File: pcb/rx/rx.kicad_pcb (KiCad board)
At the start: 2 copper layers, 82.3 x 70.8 mm, 60 parts, among them SW1 SW_SPDT, U1 nice_nano, U2 MPU-6500, U3 QMC5883P, U4 MCP6004, U5 MCP6004, U6 74HC4051

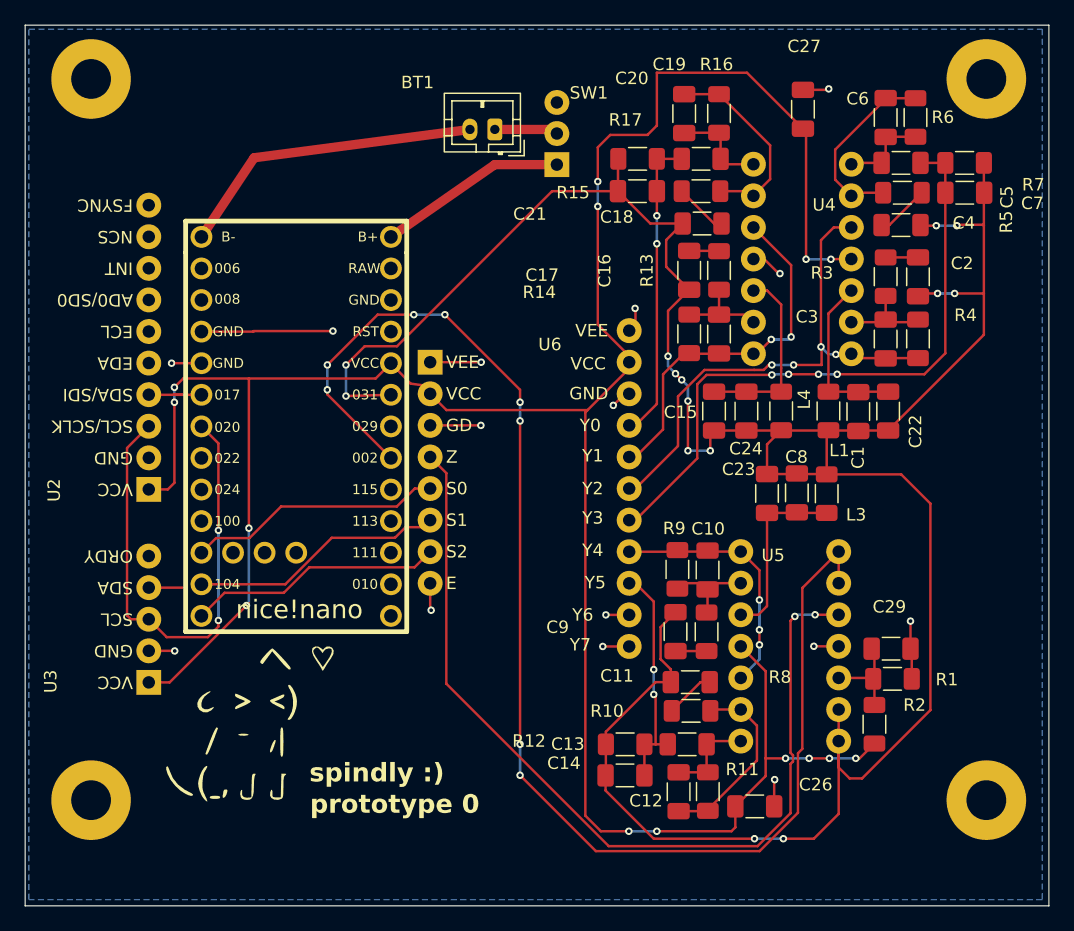
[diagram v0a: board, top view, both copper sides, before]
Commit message: Update Rx board to include anchor
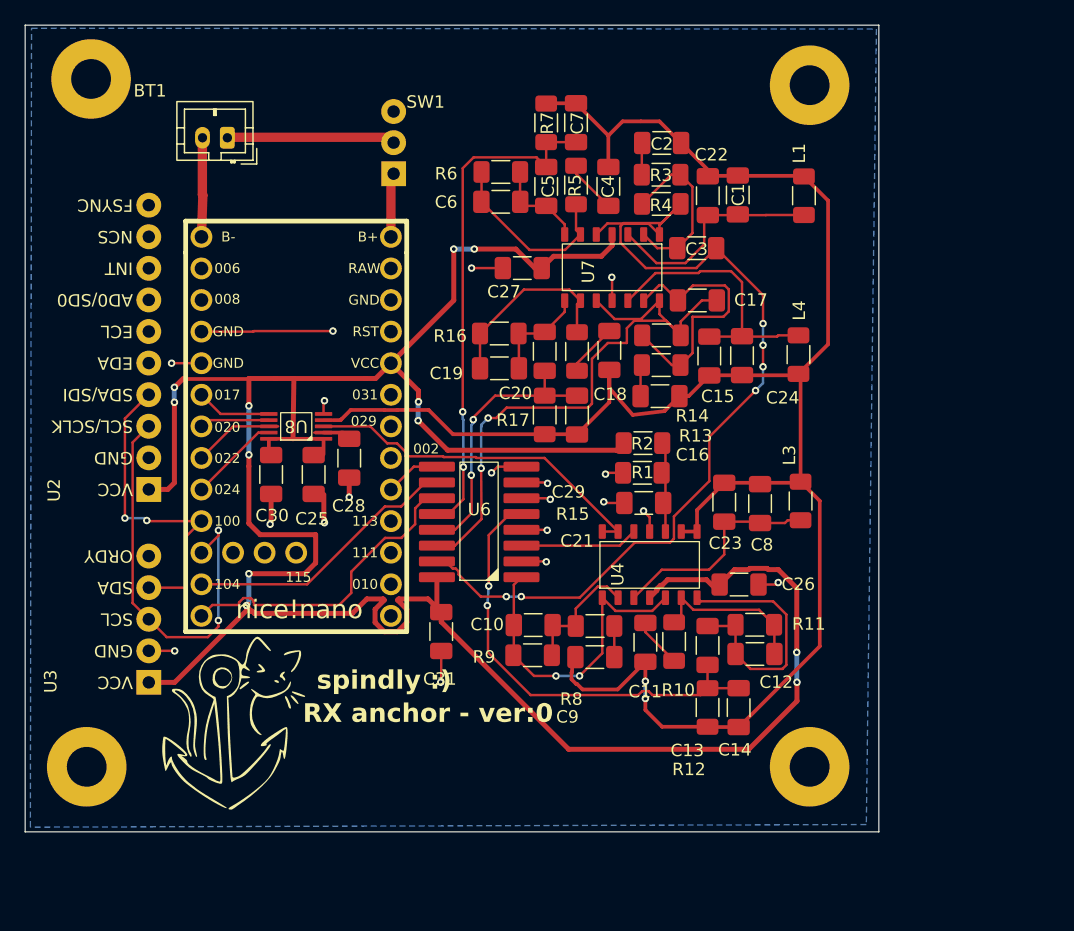
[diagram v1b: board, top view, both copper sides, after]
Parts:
- removed the G*** at (98.3, 83.4)
- removed U5: MCP6004, Library:MCP6004
- added C25: 0.1uF, Capacitor_SMD:C_1206_3216Metric_Pad1.33x1.80mm_HandSolder, F.Cu at (103.9, 63.3)
- added C28: 0.1uF, Capacitor_SMD:C_1206_3216Metric_Pad1.33x1.80mm_HandSolder, F.Cu at (106.8, 62.0)
- added C30: 0.1uF, Capacitor_SMD:C_1206_3216Metric_Pad1.33x1.80mm_HandSolder, F.Cu at (100.5, 63.3)
- added C31: 0.1uF, Capacitor_SMD:C_1206_3216Metric_Pad1.33x1.80mm_HandSolder, F.Cu at (114.2, 75.9)
- added G***: LOGO, Library:cat2_silk, F.Cu at (97.4, 83.3)
- added U7: NCS20034DR2G, Library:NCS20034DR2G, F.Cu at (127.9, 46.7)
- added U8: MCP33131-10-E/MS, Library:MCP33131, F.Cu at (102.5, 59.4)
- U4: value MCP6004 -> NCS20034DR2G; footprint Library:MCP6004 -> Library:NCS20034DR2G
- U6: footprint Library:74HC4051 -> Library:74HC4051-chip
- moved R7 33.8 mm to (122.6, 35.0), turned to 90 degrees
- moved R6 33.6 mm to (119.0, 39.0), turned to 180 degrees
- moved C7 31.8 mm to (125.0, 35.0), turned to -90 degrees
- moved C6 31.7 mm to (119.0, 41.4), turned to 0 degrees
- moved R2 29.3 mm to (130.4, 60.8), turned to 0 degrees
- moved C5 28.6 mm to (122.6, 40.1), turned to -90 degrees
- moved R5 26.3 mm to (125.0, 40.0), turned to 90 degrees
- moved R1 26.1 mm to (130.3, 63.2), turned to 180 degrees
- moved C27 25.9 mm to (120.7, 46.7), turned to 180 degrees
- moved C19 25.3 mm to (118.8, 54.8), turned to 0 degrees
- moved R16 25.0 mm to (118.8, 52.0), turned to 180 degrees
- moved C4 23.7 mm to (127.6, 40.1), turned to -90 degrees
- moved R4 23.3 mm to (131.9, 41.5), turned to 180 degrees
- moved C2 23.3 mm to (131.9, 36.6), turned to 0 degrees
- moved C29 23.1 mm to (130.4, 65.6), turned to 0 degrees
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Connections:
- C1 pad 1: Net-(U4A-+) -> Net-(U7A-+)
- C10 pad 1: Net-(U5A--) -> Net-(U4A--)
- C12 pad 1: Net-(U5B--) -> Net-(U4B--)
- C15 pad 1: Net-(U4D-+) -> Net-(U7D-+)
- C17 pad 1: Net-(U4D--) -> Net-(U7D--)
- C19 pad 1: Net-(U4C--) -> Net-(U7C--)
- C22 pad 1: Net-(U4A-+) -> Net-(U7A-+)
- C23 pad 1: Net-(U5A-+) -> Net-(U4A-+)
- C24 pad 1: Net-(U4D-+) -> Net-(U7D-+)
- C29 pad 2: Net-(U5C-+) -> Net-(U4C-+)
- C3 pad 1: Net-(U4A--) -> Net-(U7A--)
- C6 pad 1: Net-(U4B--) -> Net-(U7B--)
- C8 pad 1: Net-(U5A-+) -> Net-(U4A-+)
- L1 pad 1: Net-(U4A-+) -> Net-(U7A-+)
- L3 pad 1: Net-(U5A-+) -> Net-(U4A-+)
- L4 pad 1: Net-(U4D-+) -> Net-(U7D-+)
- R1 pad 1: Net-(U5C-+) -> Net-(U4C-+)
- R10 pad 1: Net-(U5B--) -> Net-(U4B--)
- R11 pad 2: Net-(U5B--) -> Net-(U4B--)
- R13 pad 1: Net-(U4D--) -> Net-(U7D--)
- R14 pad 2: Net-(U4D--) -> Net-(U7D--)
- R15 pad 1: Net-(U4C--) -> Net-(U7C--)
- R16 pad 2: Net-(U4C--) -> Net-(U7C--)
- R2 pad 2: Net-(U5C-+) -> Net-(U4C-+)
- R3 pad 1: Net-(U4A--) -> Net-(U7A--)
- R4 pad 2: Net-(U4A--) -> Net-(U7A--)
- R5 pad 1: Net-(U4B--) -> Net-(U7B--)
- R6 pad 2: Net-(U4B--) -> Net-(U7B--)
- R8 pad 1: Net-(U5A--) -> Net-(U4A--)
- R9 pad 2: Net-(U5A--) -> Net-(U4A--)
- U1 pad 10: /SELECT_0 -> /SCK
- U1 pad 12: /SELECT_2 -> /SELECT_0
- U1 pad 17: unconnected-(U1-P1.15-Pad17) -> /SELECT_2
- U1 pad 18: /ADC_0 -> unconnected-(U1-AIN0/P0.02-Pad18)
- U1 pad 20: /V_BIAS -> unconnected-(U1-AIN7/P0.31-Pad20)
- U1 pad 5: /SDA -> /CNVST
- U1 pad 6: /SCK -> /SDO
- U1 pad 7: unconnected-(U1-P0.22-Pad7) -> /SCLK
- U1 pad 8: unconnected-(U1-P0.24-Pad8) -> /SDI
- U1 pad 9: unconnected-(U1-P1.00-Pad9) -> /SDA
- U4 pad 1: /V_OUT3 -> /V_OUT5
- U4 pad 10: /V_OUT1 -> Net-(U4C-+)
- U4 pad 12: Net-(U4D-+) -> /ADC_BUFFER
- U4 pad 13: Net-(U4D--) -> /ADC_0
- U4 pad 14: /V_OUT1 -> /ADC_0
- U4 pad 5: /V_OUT3 -> /V_OUT5
- U4 pad 7: Net-(C5-Pad2) -> Net-(C12-Pad2)
- U4 pad 8: Net-(C19-Pad2) -> /V_BIAS
- U4 pad 9: Net-(U4C--) -> /V_BIAS
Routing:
- net /ADC_0: track 111.4 -> 28.7 mm, vias 8 -> 0
- net /ADC_BUFFER: track 72.7 -> 9.51 mm, vias 2 -> 0
- net /V_BIAS: track 214.7 -> 159.0 mm, vias 14 -> 2
- net /V_OUT3: track 42.6 -> 75.3 mm, vias 4 -> 6
- net Net-(U7D-+): track 0.00 -> 22.1 mm
- net Net-(U7D--): track 0.00 -> 21.7 mm
- net /V_OUT1: track 29.2 -> 49.6 mm
- net /V_OUT6: track 18.1 -> 36.7 mm
- net Net-(U7A-+): track 0.00 -> 17.9 mm
- net /B-: track 25.1 -> 7.99 mm
- net /SELECT_2: track 20.5 -> 4.46 mm
- net Net-(U4C--): track 16.1 -> 0.00 mm
- net Net-(U7C--): track 0.00 -> 15.4 mm
- net Net-(U5B--): track 15.2 -> 0.00 mm
- net Net-(U4D-+): track 15.1 -> 0.00 mm
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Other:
- board size 82.3 x 70.8 mm -> 68.7 x 64.9 mm
- board text added: "RX anchor - ver:0"
- board text removed: "prototype 0"

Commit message: Update
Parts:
- C4: value 0.1uF -> 0.47uF
- R3: value 750 -> 510
- R5: value 750 -> 51
